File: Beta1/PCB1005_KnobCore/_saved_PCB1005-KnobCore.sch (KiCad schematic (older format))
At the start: 41 parts, among them J1 Axoloti_40Pin, J2 FPC_20POS, U1 MCP3008T-I/SL, U10 OLED_128x32_I2C, U2 MCP3008T-I/SL, U20 OLED_128x32_I2C, U3 I2C_1x4MUX_TCA9546A, U30 OLED_128x32_I2C, U40 OLED_128x32_I2C

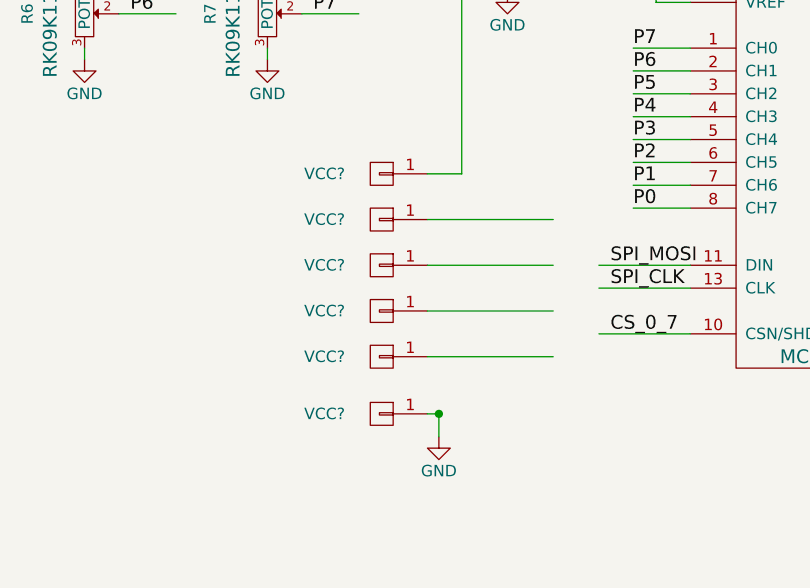
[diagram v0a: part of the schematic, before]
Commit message: Added Knobs + OLED back to PCB1005. Ready for Fab
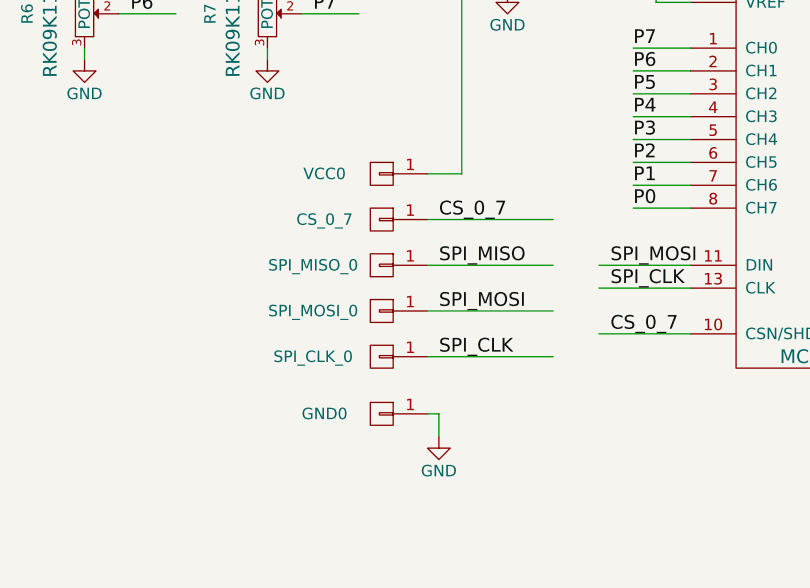
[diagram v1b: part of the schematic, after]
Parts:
- gave numbers to parts that had none: 6
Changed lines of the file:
@@
 Connection ~ 28050 10350
 $Comp
-L CONN_01X01 VCC?
+L CONN_01X01 SPI_MISO_0
 U 1 1 5993798F
 P 10750 4500
-F 0 "VCC?" H 11000 4500 50  0000 C CNN
+F 0 "SPI_MISO_0" H 11050 4500 50  0000 C CNN
 F 1 "CONN_01X01" V 10850 4500 50  0001 C CNN
 F 2 "Liberry:single_0.1" H 10750 4500 50  0001 C CNN
@@
 $EndComp
 $Comp
-L CONN_01X01 VCC?
+L CONN_01X01 CS_0_7
 U 1 1 59937BFC
 P 10750 4300
-F 0 "VCC?" H 11000 4300 50  0000 C CNN
+F 0 "CS_0_7" H 11000 4300 50  0000 C CNN
 F 1 "CONN_01X01" V 10850 4300 50  0001 C CNN
 F 2 "Liberry:single_0.1" H 10750 4300 50  0001 C CNN
@@
 $EndComp
 $Comp
-L CONN_01X01 VCC?
+L CONN_01X01 VCC0
 U 1 1 59937C85
 P 10750 4100
-F 0 "VCC?" H 11000 4100 50  0000 C CNN
+F 0 "VCC0" H 11000 4100 50  0000 C CNN
 F 1 "CONN_01X01" V 10850 4100 50  0001 C CNN
 F 2 "Liberry:single_0.1" H 10750 4100 50  0001 C CNN
@@
 $EndComp
 $Comp
-L CONN_01X01 VCC?
+L CONN_01X01 SPI_MOSI_0
 U 1 1 59937D0F
 P 10750 4700
-F 0 "VCC?" H 11000 4700 50  0000 C CNN
+F 0 "SPI_MOSI_0" H 11050 4700 50  0000 C CNN
 F 1 "CONN_01X01" V 10850 4700 50  0001 C CNN
 F 2 "Liberry:single_0.1" H 10750 4700 50  0001 C CNN
@@
 $EndComp
 $Comp
-L CONN_01X01 VCC?
+L CONN_01X01 SPI_CLK_0
 U 1 1 59937D9E
 P 10750 4900
-F 0 "VCC?" H 11000 4900 50  0000 C CNN
+F 0 "SPI_CLK_0" H 11050 4900 50  0000 C CNN
 F 1 "CONN_01X01" V 10850 4900 50  0001 C CNN
 F 2 "Liberry:single_0.1" H 10750 4900 50  0001 C CNN
@@
 $EndComp
 $Comp
-L CONN_01X01 VCC?
+L CONN_01X01 GND0
 U 1 1 59937E30
 P 10750 5150
-F 0 "VCC?" H 11000 5150 50  0000 C CNN
+F 0 "GND0" H 11000 5150 50  0000 C CNN
 F 1 "CONN_01X01" V 10850 5150 50  0001 C CNN
 F 2 "Liberry:single_0.1" H 10750 5150 50  0001 C CNN
@@
 	11100 4100 10950 4100
 $Comp
-L GND #PWR?
+L GND #PWR041
 U 1 1 59938963
 P 11000 5250
-F 0 "#PWR?" H 11000 5000 50  0001 C CNN
+F 0 "#PWR041" H 11000 5000 50  0001 C CNN
 F 1 "GND" H 11000 5100 50  0000 C CNN
 F 2 "" H 11000 5250 50  0000 C CNN
@@
 Wire Wire Line
 	11000 5250 11000 5150
-Connection ~ 11000 5150
 Wire Wire Line
 	11000 5150 10950 5150
+Text Label 11000 4900 0    60   ~ 0
+SPI_CLK
+Text Label 11000 4700 0    60   ~ 0
+SPI_MOSI
+Text Label 11000 4500 0    60   ~ 0
+SPI_MISO
+Text Label 11000 4300 0    60   ~ 0
+CS_0_7
 $EndSCHEMATC
